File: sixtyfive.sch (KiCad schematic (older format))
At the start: 204 parts, among them J1 Conn_01x12, J2 Conn_ARM_JTAG_SWD_10, Q1 BSS138, SW1 SW_Push, U1 USBLC6-2SC6, U2 STM32F072C8Tx, U3 MCP1700-3302E_SOT23

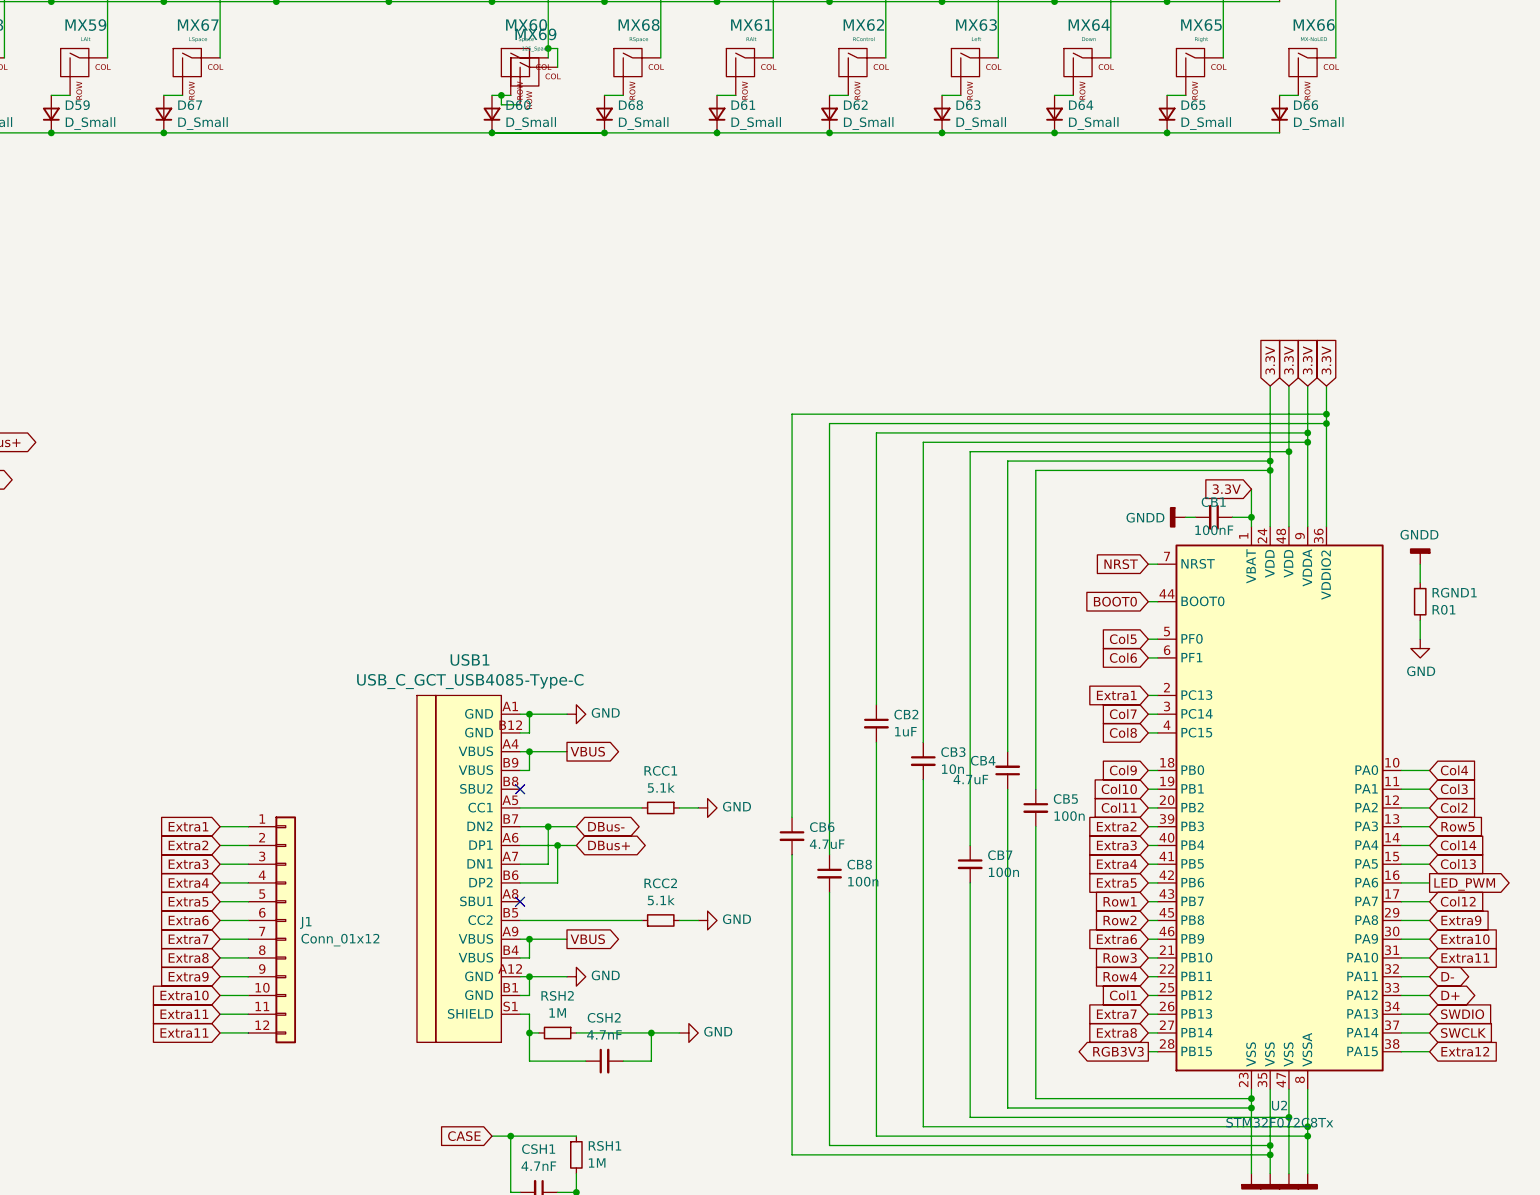
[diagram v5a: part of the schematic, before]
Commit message: Pretty sure I wired up the whole matrix
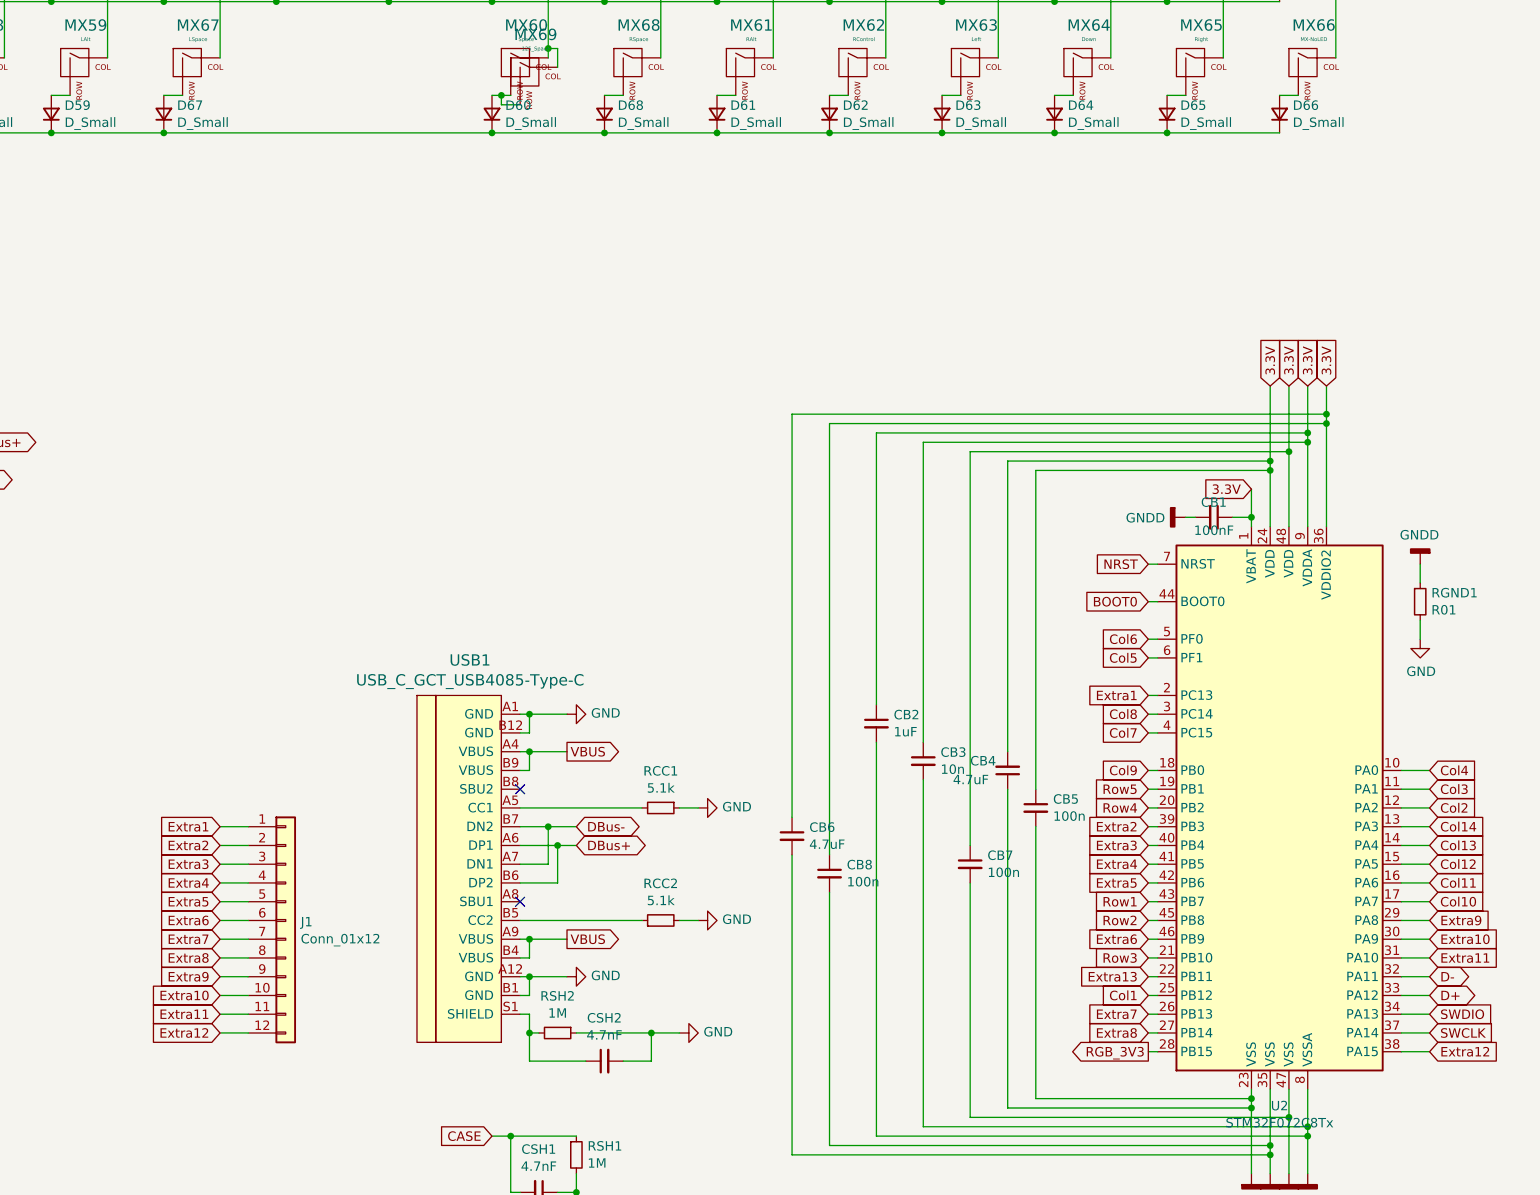
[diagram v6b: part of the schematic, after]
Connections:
- net LED_PWM is gone; now on net Col11: U2.16 (PA6)
- net RGB3V3 is gone; now on net RGB_3V3: U2.28 (PB15)
- net Col10: now also U2.17 (PA7); no longer U2.19 (PB1)
- net Col11: no longer U2.20 (PB2)
- net Col12: now also U2.15 (PA5); no longer U2.17 (PA7)
- net Col13: now also U2.14 (PA4); no longer U2.15 (PA5)
- net Col14: now also U2.13 (PA3); no longer U2.14 (PA4)
- net Col5: now also U2.6 (PF1); no longer U2.5 (PF0)
- net Col6: now also U2.5 (PF0); no longer U2.6 (PF1)
- net Col7: now also U2.4 (PC15); no longer U2.3 (PC14)
- net Col8: now also U2.3 (PC14); no longer U2.4 (PC15)
- net Extra11: no longer J1.12 (Pin_12)
- net Extra12: now also J1.12 (Pin_12)
- net Row4: now also U2.20 (PB2); no longer U2.22 (PB11)
- net Row5: now also U2.19 (PB1); no longer U2.13 (PA3)
- new net Extra13: U2.22 (PB11)
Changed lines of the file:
@@
 	28150 18500 28200 18500
 Text GLabel 28150 17100 0    50   Input ~ 0
+Col7
+Text GLabel 28150 17000 0    50   Input ~ 0
 Col8
-Text GLabel 28150 17000 0    50   Input ~ 0
-Col7
 Text GLabel 28150 16900 0    50   Input ~ 0
 Extra1
 Text GLabel 28150 16700 0    50   Input ~ 0
+Col5
+Text GLabel 28150 16600 0    50   Input ~ 0
 Col6
-Text GLabel 28150 16600 0    50   Input ~ 0
-Col5
 Text GLabel 28150 17400 0    50   Input ~ 0
-Col10
+Row5
 Text GLabel 28150 17300 0    50   Input ~ 0
 Col9
@@
 Extra2
 Text GLabel 28150 17500 0    50   Input ~ 0
-Col11
+Row4
 Text GLabel 28150 17800 0    50   Input ~ 0
 Extra4
@@
 Row2
 Text GLabel 28150 18400 0    50   Input ~ 0
-Row4
+Extra13
 Text GLabel 28150 18300 0    50   Input ~ 0
 Row3
@@
 Col1
 Text GLabel 28150 18800 0    50   Output ~ 0
-RGB3V3
+RGB_3V3
 Text GLabel 28150 18700 0    50   Input ~ 0
 Extra8
@@
 	28150 18300 28200 18300
 Text GLabel 29650 17600 2    50   Input ~ 0
-Row5
+Col14
 Wire Wire Line
 	29500 17600 29650 17600
@@
 Col2
 Text GLabel 29650 18000 2    50   Input ~ 0
+Col10
+Text GLabel 29650 17700 2    50   Input ~ 0
+Col13
+Text GLabel 29650 17800 2    50   Input ~ 0
 Col12
-Text GLabel 29650 17700 2    50   Input ~ 0
-Col14
-Text GLabel 29650 17800 2    50   Input ~ 0
-Col13
-Text GLabel 29650 17900 2    50   Output ~ 0
-LED_PWM
+Text GLabel 29650 17900 2    50   Input ~ 0
+Col11
 Text GLabel 29650 18200 2    50   Input ~ 0
 Extra10
@@
 	23200 18700 23350 18700
 Text GLabel 23200 18700 0    50   Input ~ 0
-Extra11
+Extra12
 $Comp
 L Transistor_BJT:DTC123J QRST1
@@
 	24650 13900 25250 13900
 Connection ~ 25250 13900
-Wire Wire Line
-	25250 13900 24650 13900
 $EndSCHEMATC

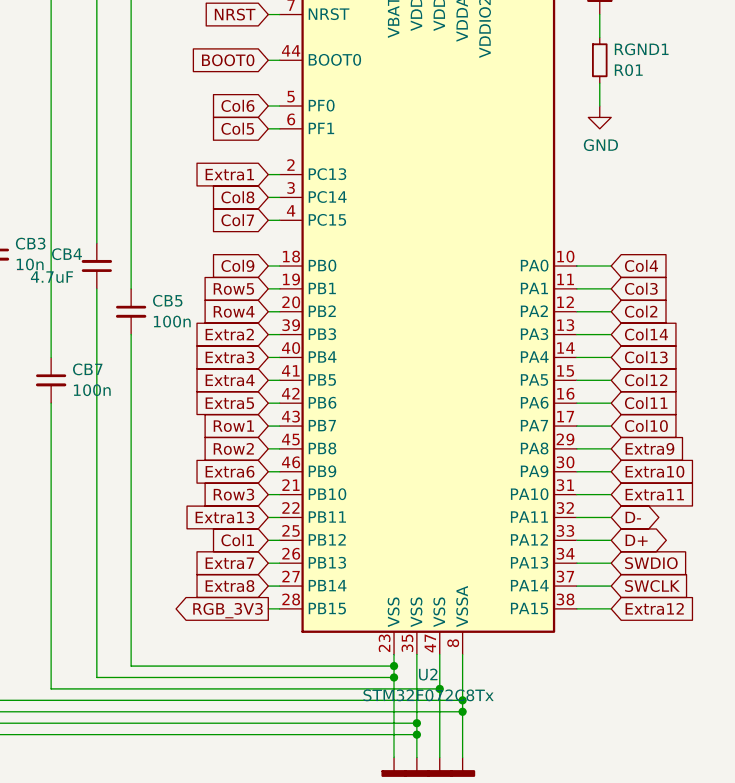
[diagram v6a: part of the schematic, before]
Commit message: extras wired up, fills started around mcu
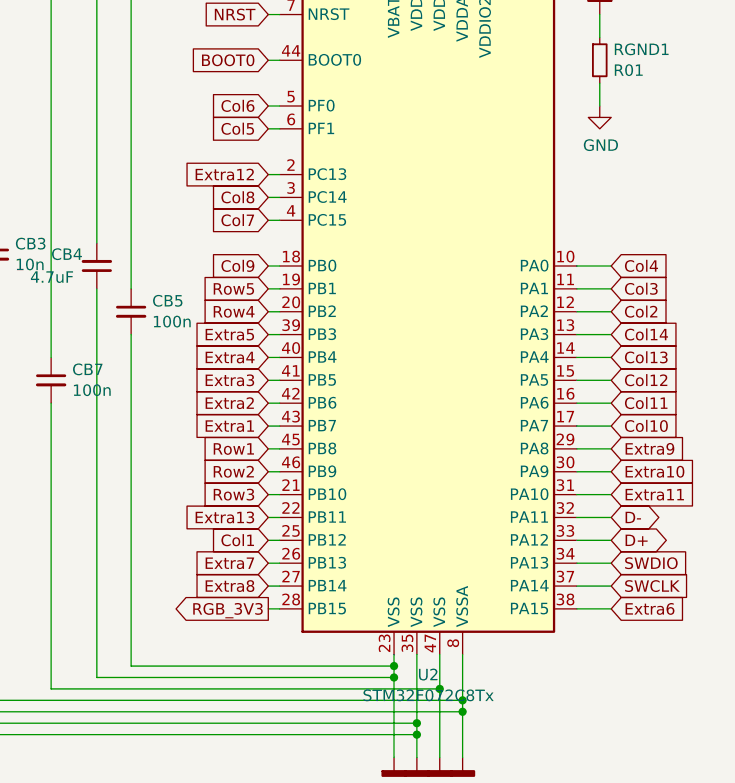
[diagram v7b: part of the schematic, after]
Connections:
- net Extra1: now also U2.43 (PB7); no longer U2.2 (PC13)
- net Extra12: now also U2.2 (PC13); no longer U2.38 (PA15)
- net Extra2: now also U2.42 (PB6); no longer U2.39 (PB3)
- net Extra3: now also U2.41 (PB5); no longer U2.40 (PB4)
- net Extra4: now also U2.40 (PB4); no longer U2.41 (PB5)
- net Extra5: now also U2.39 (PB3); no longer U2.42 (PB6)
- net Extra6: now also U2.38 (PA15); no longer U2.46 (PB9)
- net Row1: now also U2.45 (PB8); no longer U2.43 (PB7)
- net Row2: now also U2.46 (PB9); no longer U2.45 (PB8)
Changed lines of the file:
@@
 Col8
 Text GLabel 28150 16900 0    50   Input ~ 0
-Extra1
+Extra12
 Text GLabel 28150 16700 0    50   Input ~ 0
 Col5
@@
 Col9
 Text GLabel 28150 17600 0    50   Input ~ 0
-Extra2
+Extra5
 Text GLabel 28150 17500 0    50   Input ~ 0
 Row4
 Text GLabel 28150 17800 0    50   Input ~ 0
+Extra3
+Text GLabel 28150 17700 0    50   Input ~ 0
 Extra4
-Text GLabel 28150 17700 0    50   Input ~ 0
-Extra3
 Text GLabel 28150 18000 0    50   Input ~ 0
+Extra1
+Text GLabel 28150 17900 0    50   Input ~ 0
+Extra2
+Text GLabel 28150 18200 0    50   Input ~ 0
+Row2
+Text GLabel 28150 18100 0    50   Input ~ 0
 Row1
-Text GLabel 28150 17900 0    50   Input ~ 0
-Extra5
-Text GLabel 28150 18200 0    50   Input ~ 0
-Extra6
-Text GLabel 28150 18100 0    50   Input ~ 0
-Row2
 Text GLabel 28150 18400 0    50   Input ~ 0
 Extra13
@@
 Extra11
 Text GLabel 29650 18800 2    50   Input ~ 0
-Extra12
+Extra6
 Wire Wire Line
 	29650 17300 29500 17300

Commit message: Placed... everything? wired everything?
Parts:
- J2: footprint (none) -> sixtyfive:Conn_ARM_JTAG_SWD_10
- SW1: footprint (none) -> sixtyfive:smdPushBtn
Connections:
- net Extra10: now also U2.27 (PB14); no longer U2.30 (PA9)
- net Extra11: now also U2.26 (PB13); no longer U2.31 (PA10)
- net Extra12: now also U2.22 (PB11); no longer U2.2 (PC13)
- net Extra13: now also U2.2 (PC13); no longer U2.22 (PB11)
- net Extra7: now also U2.31 (PA10); no longer U2.26 (PB13)
- net Extra8: now also U2.30 (PA9); no longer U2.27 (PB14)
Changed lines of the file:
@@
 F 0 "J2" H 21557 20896 50  0000 R CNN
 F 1 "Conn_ARM_JTAG_SWD_10" H 21557 20805 50  0000 R CNN
-F 2 "" H 22000 20850 50  0001 C CNN
+F 2 "sixtyfive:Conn_ARM_JTAG_SWD_10" H 22000 20850 50  0001 C CNN
 F 3 "http://infocenter.arm.com/help/topic/com.arm.doc.ddi0314h/DDI0314H_coresight_components_trm.pdf" V 21650 19600 50  0001 C CNN
 	1    22000 20850
@@
 Col8
 Text GLabel 28150 16900 0    50   Input ~ 0
-Extra12
+Extra13
 Text GLabel 28150 16700 0    50   Input ~ 0
 Col5
@@
 Row1
 Text GLabel 28150 18400 0    50   Input ~ 0
-Extra13
+Extra12
 Text GLabel 28150 18300 0    50   Input ~ 0
 Row3
 Text GLabel 28150 18600 0    50   Input ~ 0
-Extra7
+Extra11
 Text GLabel 28150 18500 0    50   Input ~ 0
 Col1
@@
 RGB_3V3
 Text GLabel 28150 18700 0    50   Input ~ 0
-Extra8
+Extra10
 Wire Wire Line
 	28150 18800 28200 18800
@@
 Col11
 Text GLabel 29650 18200 2    50   Input ~ 0
-Extra10
+Extra8
 Text GLabel 29650 18100 2    50   Input ~ 0
 Extra9
 Text GLabel 29650 18300 2    50   Input ~ 0
-Extra11
+Extra7
 Text GLabel 29650 18800 2    50   Input ~ 0
 Extra6
@@
 F 0 "SW1" V 20346 19202 50  0000 R CNN
 F 1 "SW_Push" V 20255 19202 50  0000 R CNN
-F 2 "" H 20300 19450 50  0001 C CNN
+F 2 "sixtyfive:smdPushBtn" H 20300 19450 50  0001 C CNN
 F 3 "~" H 20300 19450 50  0001 C CNN
 	1    20300 19250
